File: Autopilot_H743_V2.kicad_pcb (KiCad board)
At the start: 6 copper layers, 50 x 50 mm, 226 parts, among them J2 XT30PW-M / 5V INPUT, J3 TYPE-C-31-M-12, J4 TF-01A / microSD, Q1 AO3401A, Q2 MMBT3906 PNP, Q3 MMBT2222A NPN, SW1 RESET, SW2 BOOT, U1 STM32H743VIT6, U10 BMI088, U11 MMC5983MA, U12 SPA06-003, U13 USBLC6-2SC6, U14 USBLC6-2SC6, U15 USBLC6-2SC6, U16 USBLC6-2SC6, U17 USBLC6-2SC6, U18 USBLC6-2SC6, U19 TPS2553DBVR, U2 AP63203WU-7, U20 USBLC6-2SC6, U21 SN74LV8T245PWR, U22 TMUX1574PWR, U23 TMUX1574PWR, U3 TPS2113APWR, U4 TPS7A2033PDBVR, U5 TUSB320LIRWBR, U6 TPS2553DBVR, U7 USBLC6-2SC6, U8 USBLC6-2SC6, U9 TPS7A2033PDBVR, Y1 8MHz

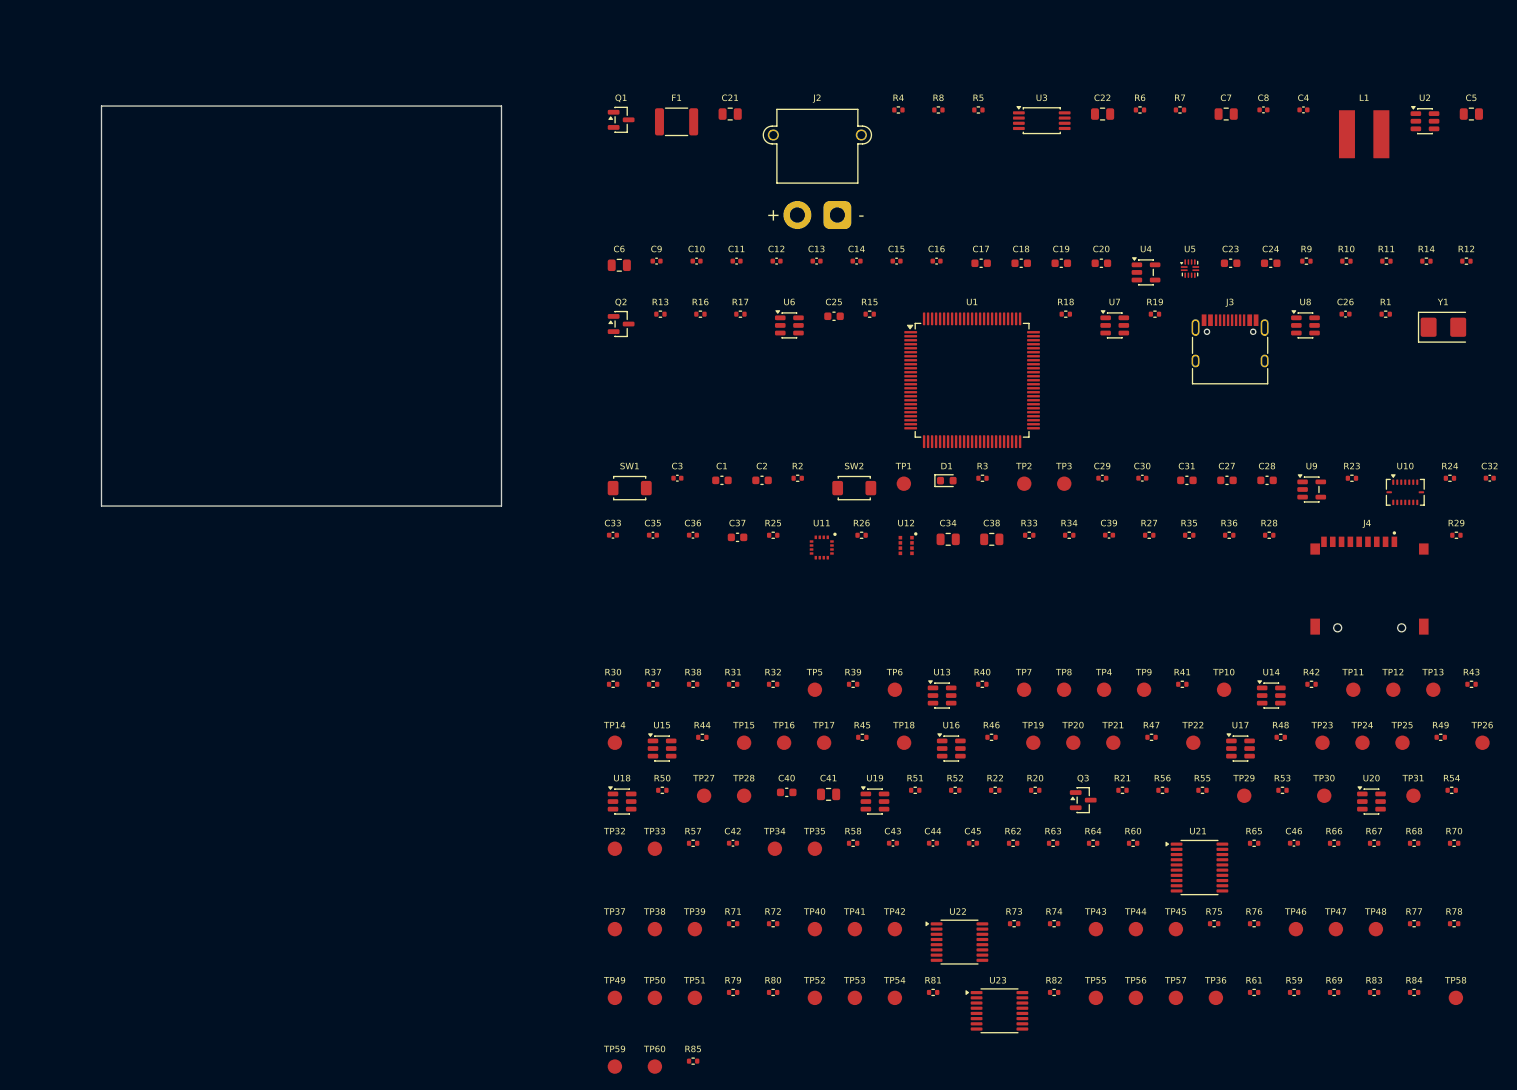
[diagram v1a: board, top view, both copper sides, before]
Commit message: Shrink v2 solder pads and place peripherals with M3 mounting
Use underside 1.2 mm signal and 1.5 mm power/ground pads, a 40 mm placement target and 30.5 mm mounting centres. Correct XT30 sourcing to AMASS XT30PW-M30.G.Y / C431092. Preserve existing internal footprint arrangement and project constraints.

ERC and schematic parity pass. DRC has NOT passed: 487 unconnected items remain, with internal placement and all routing still pending. Add top/bottom peripheral placement preview with simplified connector bodies.
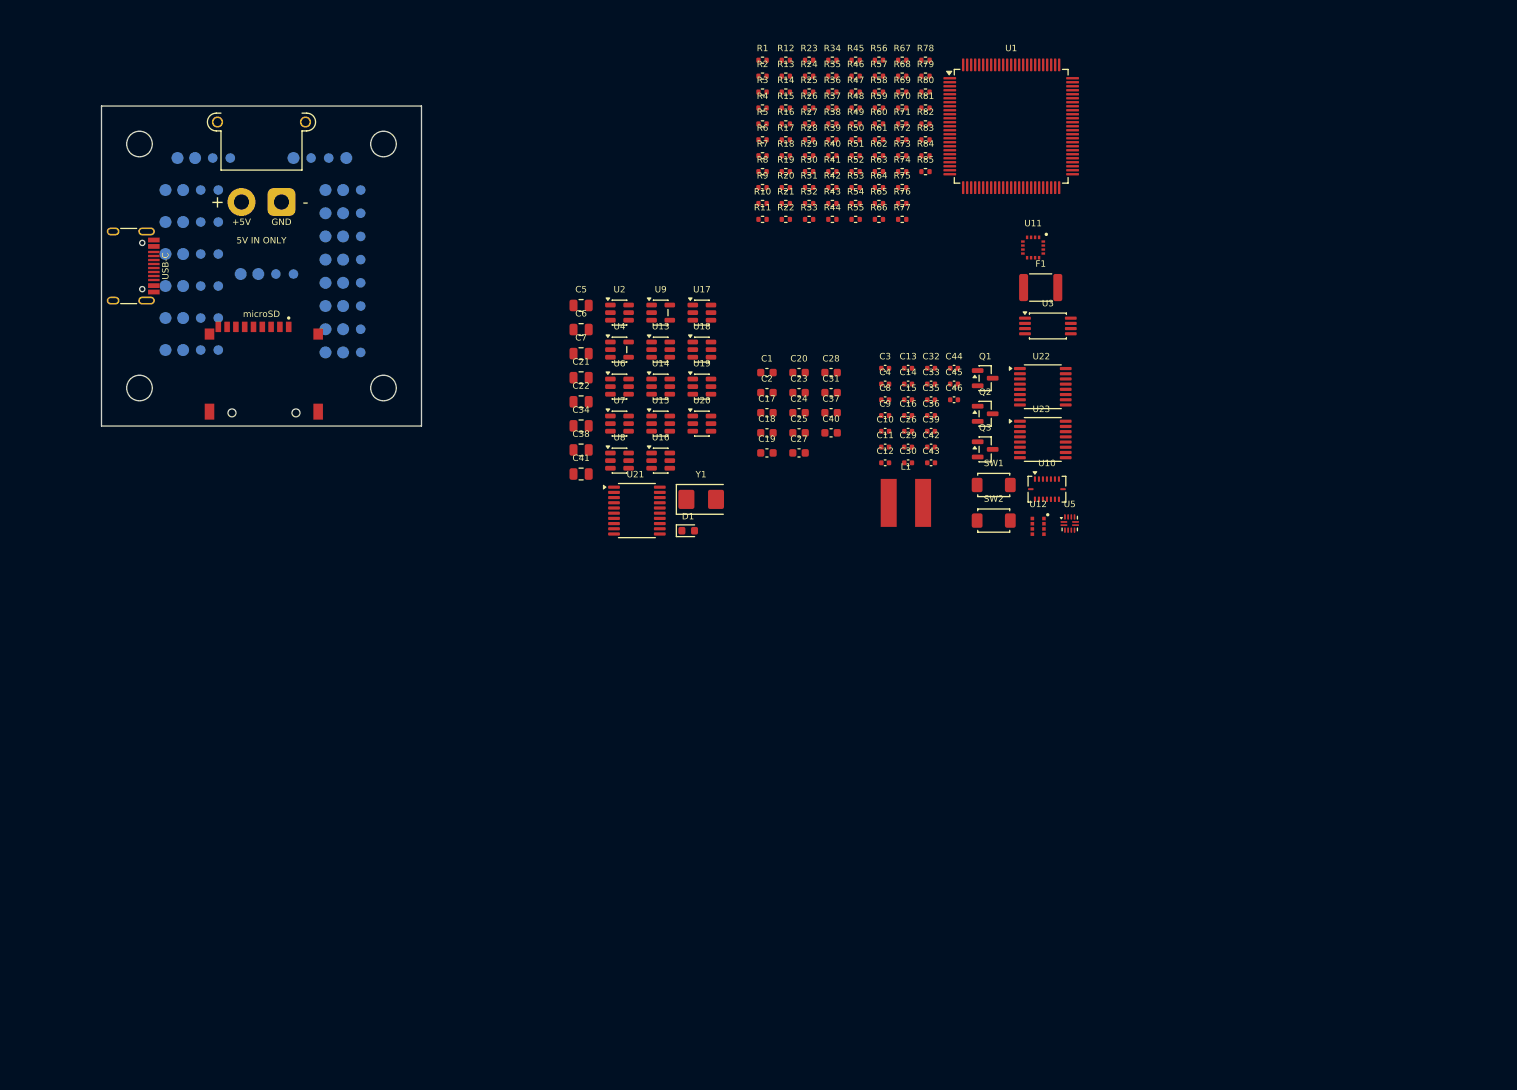
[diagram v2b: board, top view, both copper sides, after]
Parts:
- added H1: M3 / 30.5mm centres, Autopilot_H743_V2:MountingHole_3.2mm_M3, F.Cu at (104.8, 104.8)
- added H2: M3 / 30.5mm centres, Autopilot_H743_V2:MountingHole_3.2mm_M3, F.Cu at (135.2, 104.8)
- added H3: M3 / 30.5mm centres, Autopilot_H743_V2:MountingHole_3.2mm_M3, F.Cu at (135.2, 135.2)
- added H4: M3 / 30.5mm centres, Autopilot_H743_V2:MountingHole_3.2mm_M3, F.Cu at (104.8, 135.2)
- TP1, TP12, TP13, TP16, TP17, TP20, TP21, TP24, TP25, TP28, TP29, TP32, TP33, TP36, TP37, TP38, TP4, TP40, TP41, TP43, TP44, TP46, TP47, TP49, TP5, TP50, TP52, TP53, TP55, TP56, TP58, TP59, TP8, TP9: footprint Autopilot_H743_V2:SolderPad_D1.8mm -> Autopilot_H743_V2:SolderPad_D1.5mm; moved to B.Cu
- TP10, TP11, TP14, TP15, TP18, TP19, TP2, TP22, TP23, TP26, TP27, TP3, TP30, TP31, TP34, TP35, TP39, TP42, TP45, TP48, TP51, TP54, TP57, TP6, TP60, TP7: footprint Autopilot_H743_V2:SolderPad_D1.8mm -> Autopilot_H743_V2:SolderPad_D1.2mm; moved to B.Cu
- moved TP31 168.0 mm to (116.1, 106.5)
- moved TP26 167.6 mm to (112.4, 130.5)
- moved TP13 165.5 mm to (110.2, 118.5)
- moved TP12 164.2 mm to (108.0, 114.5)
- moved TP58 162.7 mm to (128.0, 130.8)
- moved TP30 160.2 mm to (113.9, 106.5)
- moved TP25 160.1 mm to (110.2, 130.5)
- moved TP24 158.8 mm to (108.0, 126.5)
- moved TP29 153.5 mm to (111.7, 106.5)
- moved TP11 153.4 mm to (114.6, 114.5)
- moved TP48 152.0 mm to (132.4, 119.2)
- moved TP36 151.1 mm to (130.6, 106.5)
- moved TP47 149.7 mm to (130.2, 119.2)
- moved TP23 147.9 mm to (114.6, 126.5)
- moved TP46 147.4 mm to (128.0, 119.2)
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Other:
- board size 50 x 50 mm -> 40 x 40 mm
- board text added: "+5V"
- board text added: "1"
- board text added: "2"
- board text added: "3"
- board text added: "3V3"
- board text added: "4"
- board text added: "5"
- board text added: "5V"
- board text added: "5V = PERIPH"
- board text added: "5V IN ONLY"
- board text added: "6"
- board text added: "7"
- board text added: "8"
- board text added: "BI"
- board text added: "BV"
- board text added: "CL"
- board text added: "CLK"
- board text added: "DA"
- board text added: "DIO"
- board text added: "G"
- board text added: "GND"
- board text added: "OUT 1-8"
- board text added: "Peripheral placement proposal; internals unplaced / unrouted. 30.5 mm M3 mounting centres; solder pads on B.Cu. XT30: regulated 5 V BEC input only."
- board text added: "RX"
- board text added: "S"
- board text added: "SWD"
- board text added: "TX"
- board text added: "U1"
- board text added: "U2"
- board text added: "U3"
- board text added: "U6"
- board text added: "U7"
- board text added: "U8"
- board text added: "USB-C"
- board text added: "V2 / 40 x 40 mm PLACEMENT TARGET"
- board text added: "V2 / BOTTOM"
- board text added: "VS"
- board text added: "VS: SERVO"
- board text added: "microSD"
- board text removed: "Placement and routing not started. Board size is a target, not a verified fit. XT30: regulated 5 V BEC input only."
- board text removed: "V2 / 50 x 50 mm TARGET"

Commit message: Use solder-pad 5V input and shared servo supply; DRC not passed
Replace XT30 with ordinary 4 x 4 mm power pads. Feed servo power from V5_MAIN_IN before avionics protection, retaining USB-only logic power. Add C47 local decoupling and power routing notes/preset. ERC and schematic parity pass; board remains unrouted with 490 unconnected items and 282 parked-component DRC violations.
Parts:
- added C47: 47uF, Autopilot_H743_V2:Capacitor_SMD__C_1206_3216Metric, F.Cu at (130.0, 111.0)
- J2: value XT30PW-M / 5V INPUT -> 5V BEC INPUT PADS; footprint Autopilot_H743_V2:AMASS_XT30PW-M_1x02_P2.50mm_Horizontal -> Autopilot_H743_V2:PowerInput_2Pad_4x4mm_P7mm
- TP38, TP41, TP44, TP47, TP50, TP53, TP56, TP59: value V_SERVO_BEC -> V5_MAIN_IN
- moved J2 9.58 mm to (120.0, 102.8)
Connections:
- TP38 pad 1: /V_SERVO_BEC -> /V5_MAIN_IN
- TP41 pad 1: /V_SERVO_BEC -> /V5_MAIN_IN
- TP44 pad 1: /V_SERVO_BEC -> /V5_MAIN_IN
- TP47 pad 1: /V_SERVO_BEC -> /V5_MAIN_IN
- TP50 pad 1: /V_SERVO_BEC -> /V5_MAIN_IN
- TP53 pad 1: /V_SERVO_BEC -> /V5_MAIN_IN
- TP56 pad 1: /V_SERVO_BEC -> /V5_MAIN_IN
- TP59 pad 1: /V_SERVO_BEC -> /V5_MAIN_IN
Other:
- board text added: "5V BEC INPUT"
- board text added: "Peripheral placement proposal; internals unplaced / unrouted. 30.5 mm M3 mounting centres; TP solder pads on B.Cu. J2: ordinary 4 x 4 mm top pads, 0.75 mm inside north edge; no paste. Regulated 5 V BEC powers avionics and servos; USB does not power servos. Servo current bypasses F1 / Q1 / U3. No servo fuse or reverse protection. Use broad +5V / GND copper; validate current, voltage drop and BEC t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"
- board text added: "SERVO: BEC"
- board text added: "UART: 5V"
- board text removed: "5V = PERIPH"
- board text removed: "5V IN ONLY"
- board text removed: "Peripheral placement proposal; internals unplaced / unrouted. 30.5 mm M3 mounting centres; solder pads on B.Cu. XT30: regulated 5 V BEC input only."
- board text removed: "VS"
- board text removed: "VS: SERVO"

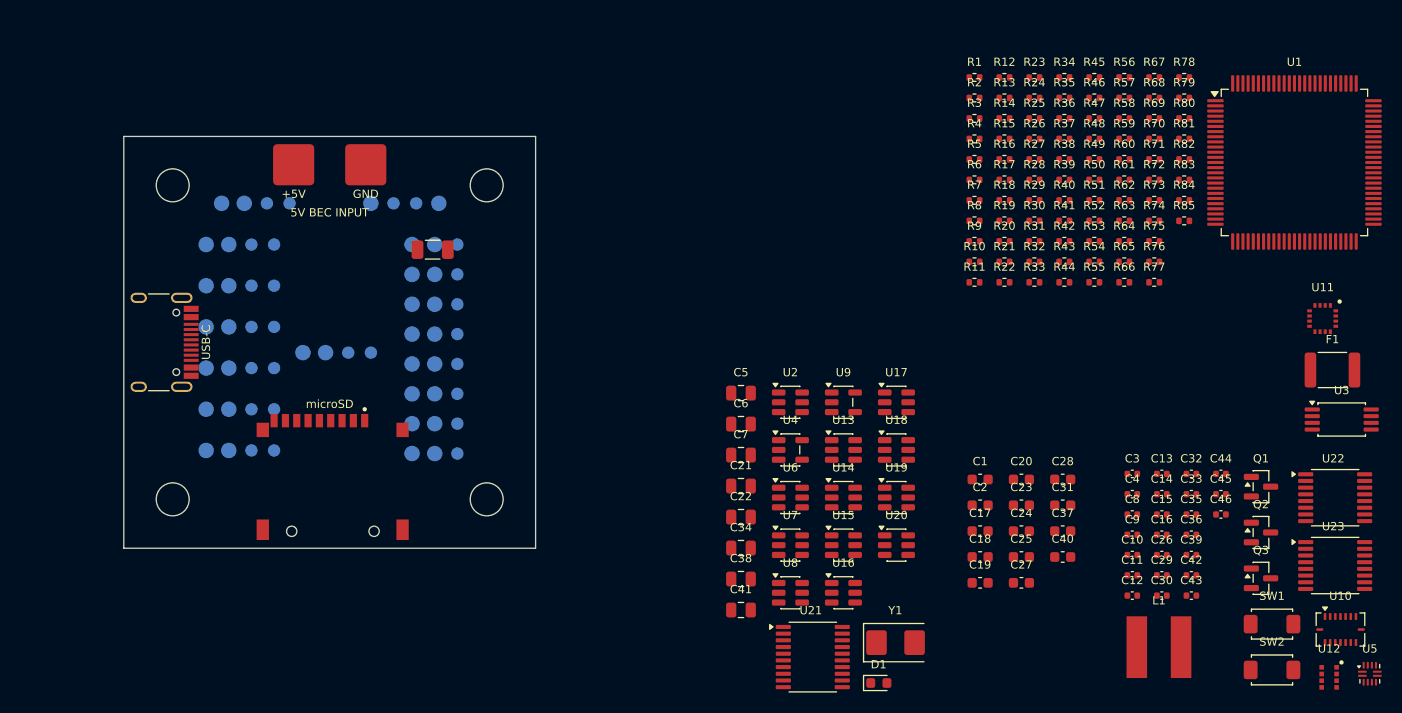
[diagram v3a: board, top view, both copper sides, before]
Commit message: Expand v2 to 60mm with 50mm M3 mounting; DRC not passed
Redistribute underside peripheral pads at 3mm column pitch, 7mm UART row pitch and 5mm servo row pitch. Move power pads, USB-C and microSD to the new edges. Preserve the saved internal placements and project settings. ERC passes and all 180 nets are unchanged; internal placement and routing remain unfinished, with 490 unconnected items.
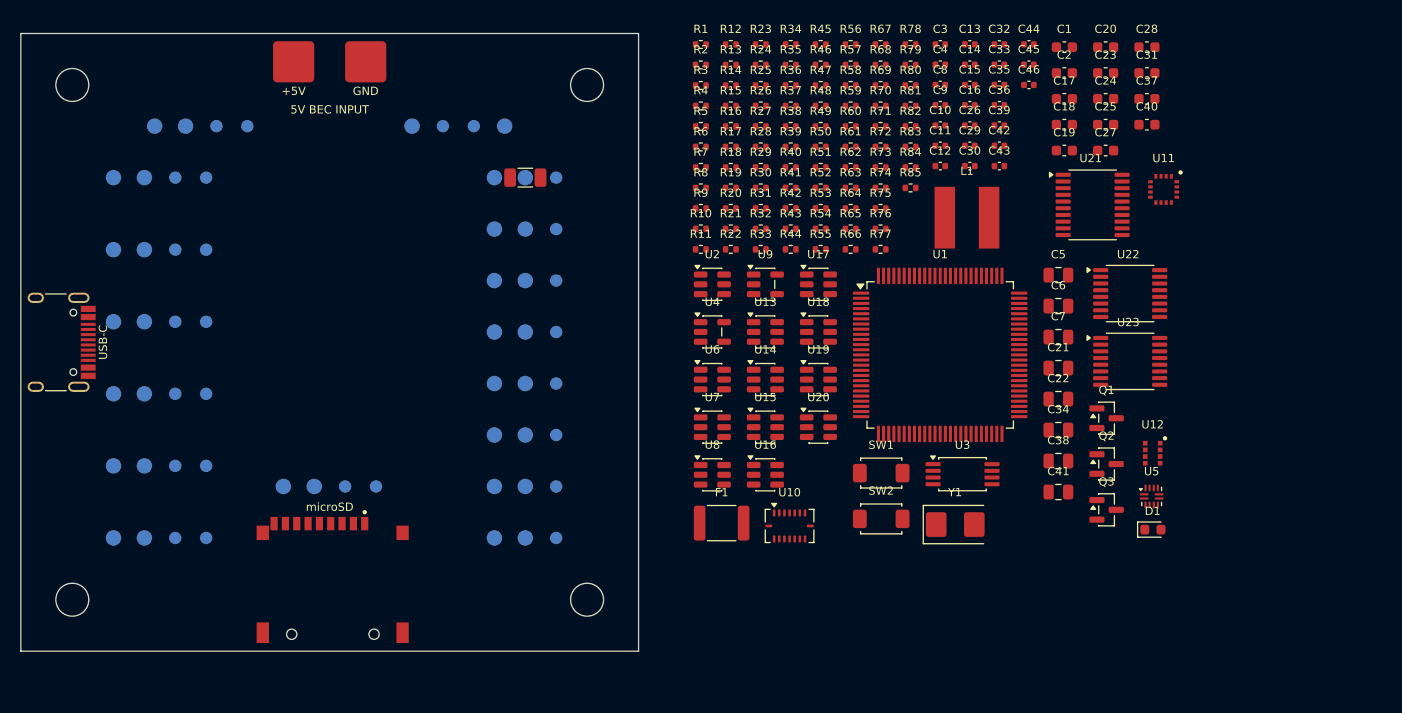
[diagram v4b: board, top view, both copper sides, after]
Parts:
- H1, H2, H3, H4: value M3 / 30.5mm centres -> M3 / 50mm centres
- moved F1 61.2 mm to (158.1, 137.6)
- moved U10 54.4 mm to (164.7, 137.8)
- moved U21 51.6 mm to (194.1, 106.7)
- moved L1 45.7 mm to (181.9, 107.9)
- moved C10 45.7 mm to (179.3, 98.9)
- moved C11 45.7 mm to (179.3, 100.9)
- moved C12 45.7 mm to (179.3, 102.9)
- moved C13 45.7 mm to (182.2, 91.1)
- moved C14 45.7 mm to (182.2, 93.0)
- moved C15 45.7 mm to (182.2, 95.0)
- moved C16 45.7 mm to (182.2, 97.0)
- moved C26 45.7 mm to (182.2, 98.9)
- moved C29 45.7 mm to (182.2, 100.9)
- moved C3 45.7 mm to (179.3, 91.1)
- moved C30 45.7 mm to (182.2, 102.9)
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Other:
- board size 40 x 40 mm -> 60 x 60 mm
- board text added: "BATT MON"
- board text added: "I2C"
- board text removed: "Peripheral placement proposal; internals unplaced / unrouted. 30.5 mm M3 mounting centres; TP solder pads on B.Cu. J2: ordinary 4 x 4 mm top pads, 0.75 mm inside north edge; no paste. Regulated 5 V BEC powers avionics and servos; USB does not power servos. Servo current bypasses F1 / Q1 / U3. No servo fuse or reverse protection. Use broad +5V / GND copper; validate current, voltage drop and BEC t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"
- board text removed: "UNPLACED FOOTPRINTS — arrange on board before routing"
- board text removed: "V2 / 40 x 40 mm PLACEMENT TARGET"
